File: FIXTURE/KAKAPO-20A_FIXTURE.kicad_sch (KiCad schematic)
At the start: 58 parts, among them J1 Conn_01x03, J10 Pins_2.54_1x2, J2 Conn_01x03, J3 Conn_01x03, J4 Conn_01x03, J5 Pins_2.54_1x2, J7 Conn_01x03, J8 Conn_01x03, M1 Mount_M3, M10 Mount_M3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

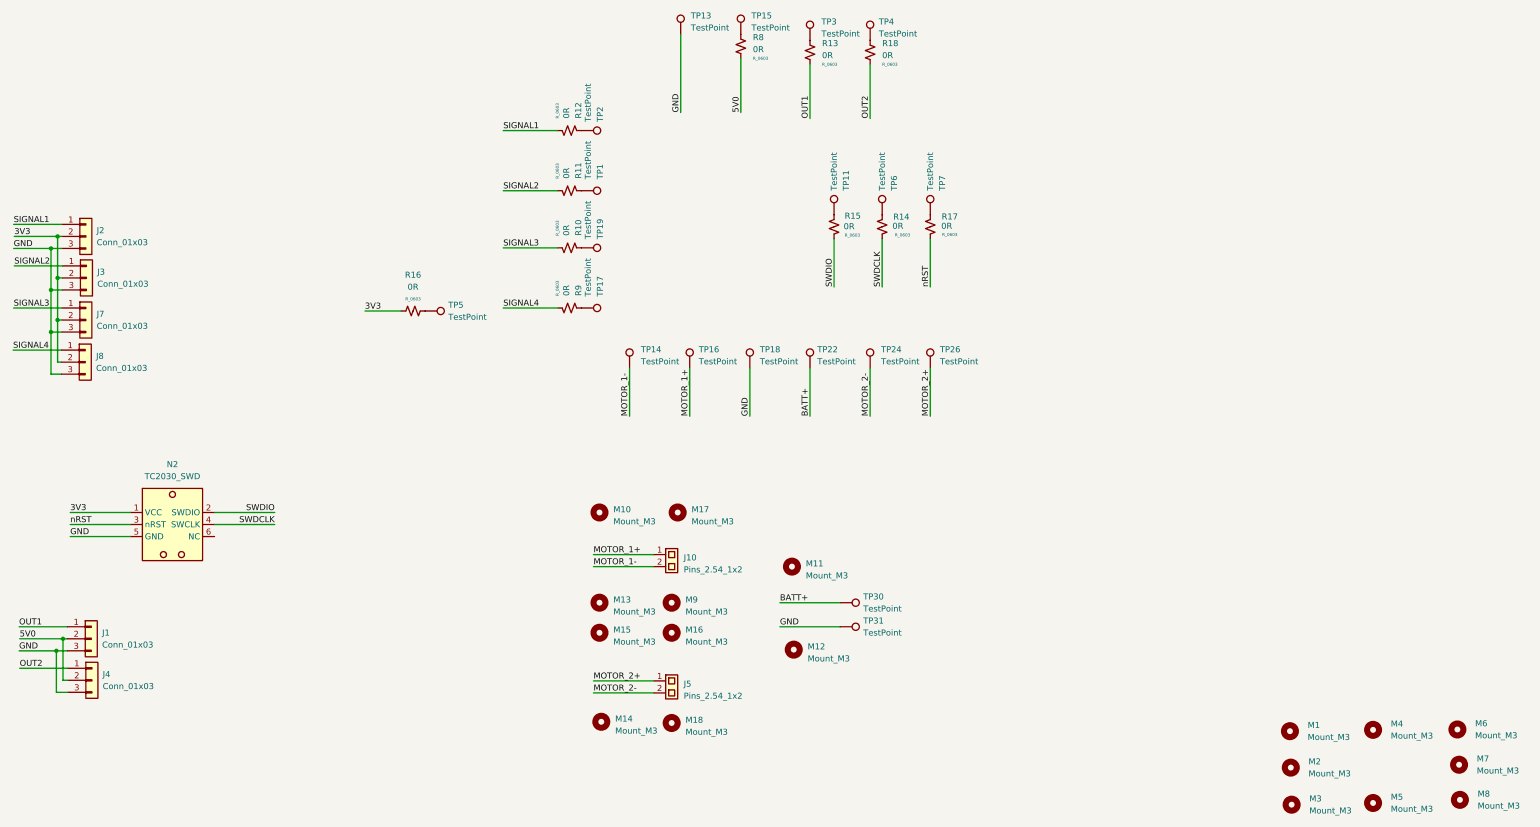
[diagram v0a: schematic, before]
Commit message: Update Fixture Design to Be Inline With Other Jigs
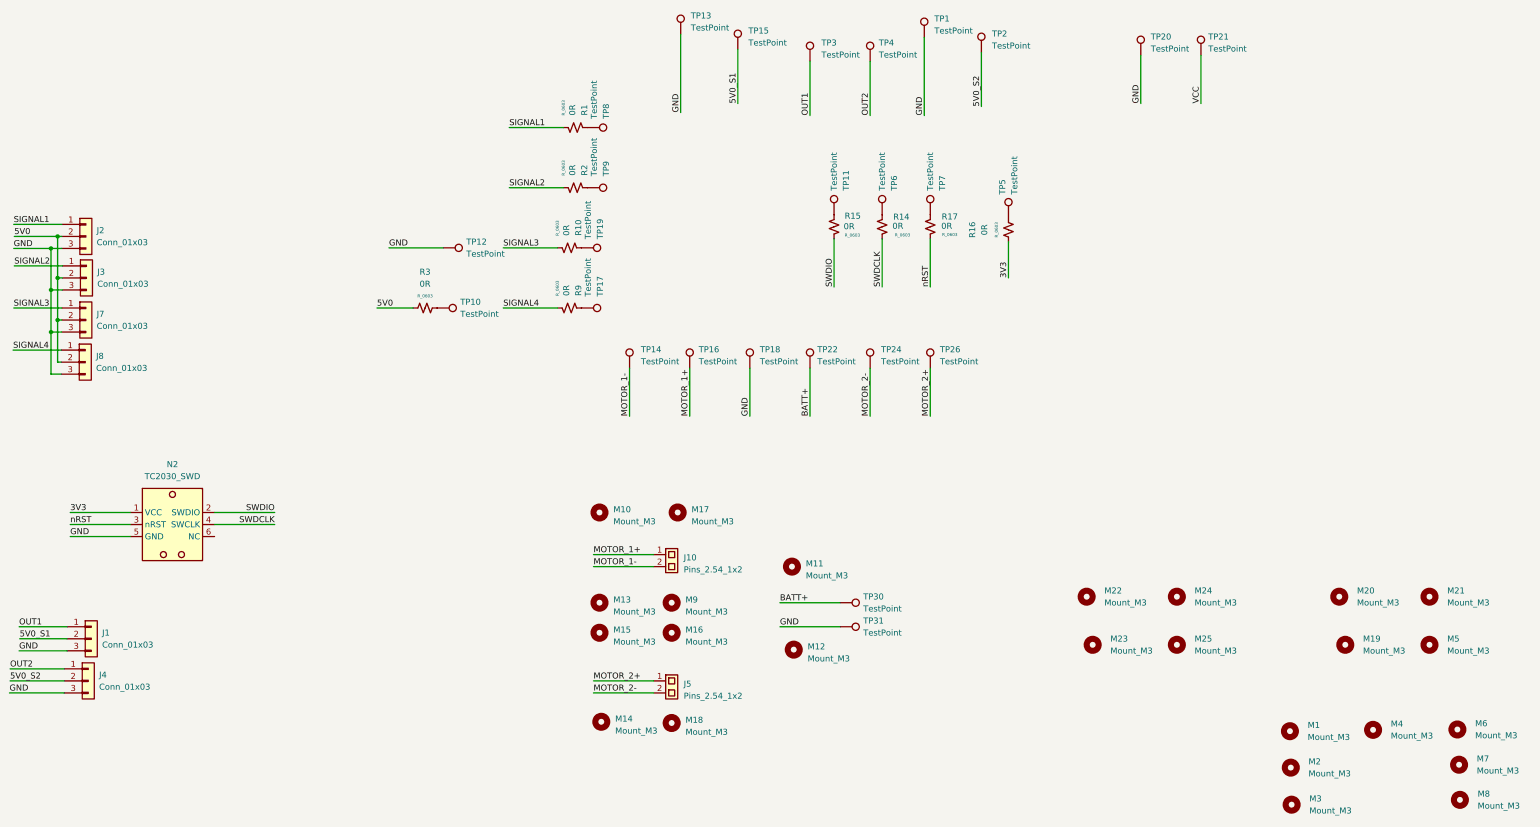
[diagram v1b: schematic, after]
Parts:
- removed R11, R12, R13, R18, R8: 0R, R_Resistor:R_0603, symbol .R_Resistor:R_0603
- added M19, M20, M21, M22, M23, M24, M25: Mount_M3, M_Mechanical:Mount_M3, symbol .M_Mechanical:Mount_M3
- added R1, R2, R3: 0R, R_Resistor:R_0603, symbol .R_Resistor:R_0603
- added TP10, TP12, TP20, TP21, TP8, TP9: TestPoint, TestPoint:TestPoint_THTPad_D3.0mm_Drill1.5mm, symbol Connector:TestPoint
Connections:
- net 3V3: no longer J2.2 (Pin_2), J3.2 (Pin_2), J7.2 (Pin_2), J8.2 (Pin_2)
- net 5V0: now also J2.2 (Pin_2), J3.2 (Pin_2), J7.2 (Pin_2), J8.2 (Pin_2), R3.1; no longer J1.2 (Pin_2), J4.2 (Pin_2)
- net GND: now also TP1.1, TP12.1, TP20.1
- net OUT1: now also TP3.1
- net OUT2: now also TP4.1
- net SIGNAL1: now also R1.2
- net SIGNAL2: now also R2.2
- net 5V0_S1: now reaches TP15.1
- net 5V0_S1: now also J1.2 (Pin_2)
- net 5V0_S2: now reaches TP2.1
- net 5V0_S2: now also J4.2 (Pin_2)
- new net: R3.2, TP10.1
- new net: R1.1, TP8.1
- new net: R2.1, TP9.1
- new net VCC: TP21.1
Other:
- moved on the sheet: J4, R16, TP15, TP3, TP4, TP5
